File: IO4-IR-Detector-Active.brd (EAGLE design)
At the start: 50 x 50 mm, 32 parts, among them Q1 NPN-2222, Q2 NPN-2222, Q3 NPN-2222, Q4 NPN-2222

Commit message: panelized
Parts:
- C3: device SPCoast:E2-5 -> SPCoast:0810-CAP
- moved LED1 7.62 mm to (14.0, 3.81), turned to 270 degrees
- moved LED4 7.62 mm to (6.35, 3.81), turned to 270 degrees
- moved R12 7.62 mm to (6.35, 8.26)
- moved R9 7.62 mm to (14.0, 8.26)
- moved C3 4.84 mm to (38.6, 4.83)
- moved LED2 2.54 mm to (11.4, 3.81), turned to 270 degrees
- moved LED3 2.54 mm to (8.89, 3.81), turned to 270 degrees
- moved R10 2.54 mm to (11.4, 8.26)
- moved R11 2.54 mm to (8.89, 8.26)
- moved Q2 1.42 mm to (29.2, 39.4), turned to 180 degrees
- moved R2 1.27 mm to (40.0, 35.6)
- moved R6 1.27 mm to (34.9, 35.6)
- moved JP2 1.27 mm to (42.5, 31.8)
- moved JP3 1.27 mm to (42.5, 21.6)
- moved JP4 1.27 mm to (42.5, 11.4)
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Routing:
- net GND: track 31.4 -> 54.8 mm, vias 8 -> 4
- net V+: track 164.3 -> 175.8 mm
- net L1: track 17.6 -> 10.7 mm
- net L2: track 20.6 -> 14.3 mm
- net L3: track 21.5 -> 17.9 mm
- net IR4: track 58.8 -> 56.0 mm
- net IRSIG4: track 45.2 -> 43.0 mm
- net IRSIG1: track 34.5 -> 32.6 mm, vias 1 -> 2
- net IR3: track 51.9 -> 50.0 mm
- net IRSIG3: track 28.6 -> 27.5 mm
- net IRDRIVE1: track 11.1 -> 10.0 mm
- net IR2: track 41.6 -> 40.9 mm
- net IRDRIVE2: track 11.6 -> 10.9 mm
- net IRSIG2: track 18.7 -> 19.2 mm
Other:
- outline, holes or cut-outs redrawn
- board text added: "C1"
- board text added: "C2"
- board text added: "C3"
- board text added: "CON1"
- board text added: "JP1"
- board text added: "JP2"
- board text added: "JP3"
- board text added: "JP4"
- board text added: "LED1"
- board text added: "LED2"
- board text added: "LED3"
- board text added: "LED4"
- board text added: "LED5"
- board text added: "Q1"
- board text added: "Q2"
- board text added: "Q3"
- board text added: "Q4"
- board text added: "R1"
- board text added: "R10"
- board text added: "R11"
- board text added: "R12"
- board text added: "R14"
- board text added: "R2"
- board text added: "R3"
- board text added: "R4"
- board text added: "R5"
- board text added: "R6"
- board text added: "R7"
- board text added: "R8"
- board text added: "R9"

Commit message: added values for connectors
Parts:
- CON1: value (none) -> RJ12/6
- JP1, JP2, JP3, JP4: value (none) -> 0.100
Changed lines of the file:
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@@
 <attribute name="VALUE" x="33.782" y="44.831" size="0.8128" layer="27" rot="R180"/>
 </element>
-<element name="JP1" library="SPCoast" package="1X04_LOCK" value="" x="42.545" y="41.91" smashed="yes" rot="R180">
+<element name="JP1" library="SPCoast" package="1X04_LOCK" value="0.100" x="42.545" y="41.91" smashed="yes" rot="R180">
 <attribute name="NAME" x="43.8912" y="44.9072" size="0.8128" layer="25" ratio="10" rot="R180"/>
 <attribute name="VALUE" x="43.815" y="45.085" size="1.27" layer="27" rot="R180"/>
 </element>
-<element name="JP2" library="SPCoast" package="1X04_LOCK" value="" x="42.545" y="31.75" smashed="yes" rot="R180">
+<element name="JP2" library="SPCoast" package="1X04_LOCK" value="0.100" x="42.545" y="31.75" smashed="yes" rot="R180">
 <attribute name="NAME" x="44.3992" y="34.4932" size="0.8128" layer="25" ratio="10" rot="R180"/>
 <attribute name="VALUE" x="43.815" y="34.925" size="1.27" layer="27" rot="R180"/>
@@
 <attribute name="VALUE" x="33.782" y="24.384" size="0.8128" layer="27" rot="R180"/>
 </element>
-<element name="JP3" library="SPCoast" package="1X04_LOCK" value="" x="42.545" y="21.59" smashed="yes" rot="R180">
+<element name="JP3" library="SPCoast" package="1X04_LOCK" value="0.100" x="42.545" y="21.59" smashed="yes" rot="R180">
 <attribute name="NAME" x="44.3992" y="24.3332" size="0.8128" layer="25" ratio="10" rot="R180"/>
 <attribute name="VALUE" x="43.815" y="24.765" size="1.27" layer="27" rot="R180"/>
 </element>
-<element name="JP4" library="SPCoast" package="1X04_LOCK" value="" x="42.545" y="11.43" smashed="yes" rot="R180">
+<element name="JP4" library="SPCoast" package="1X04_LOCK" value="0.100" x="42.545" y="11.43" smashed="yes" rot="R180">
 <attribute name="NAME" x="44.1452" y="14.4272" size="0.8128" layer="25" ratio="10" rot="R180"/>
 <attribute name="VALUE" x="43.815" y="14.605" size="1.27" layer="27" rot="R180"/>
@@
 <attribute name="VALUE" x="16.51" y="44.831" size="1.016" layer="27" rot="R180"/>
 </element>
-<element name="CON1" library="SPCoast" package="RJ25-PANEL" value="" x="22.86" y="3.175">
+<element name="CON1" library="SPCoast" package="RJ25-PANEL" value="RJ12/6" x="22.86" y="3.175">
 <attribute name="AMP" value="520250-3" x="22.86" y="3.175" size="1.778" layer="27" font="vector" ratio="10" display="off"/>
 <attribute name="OPL" value="none" x="22.86" y="3.175" size="1.778" layer="27" font="vector" ratio="10" display="off"/>

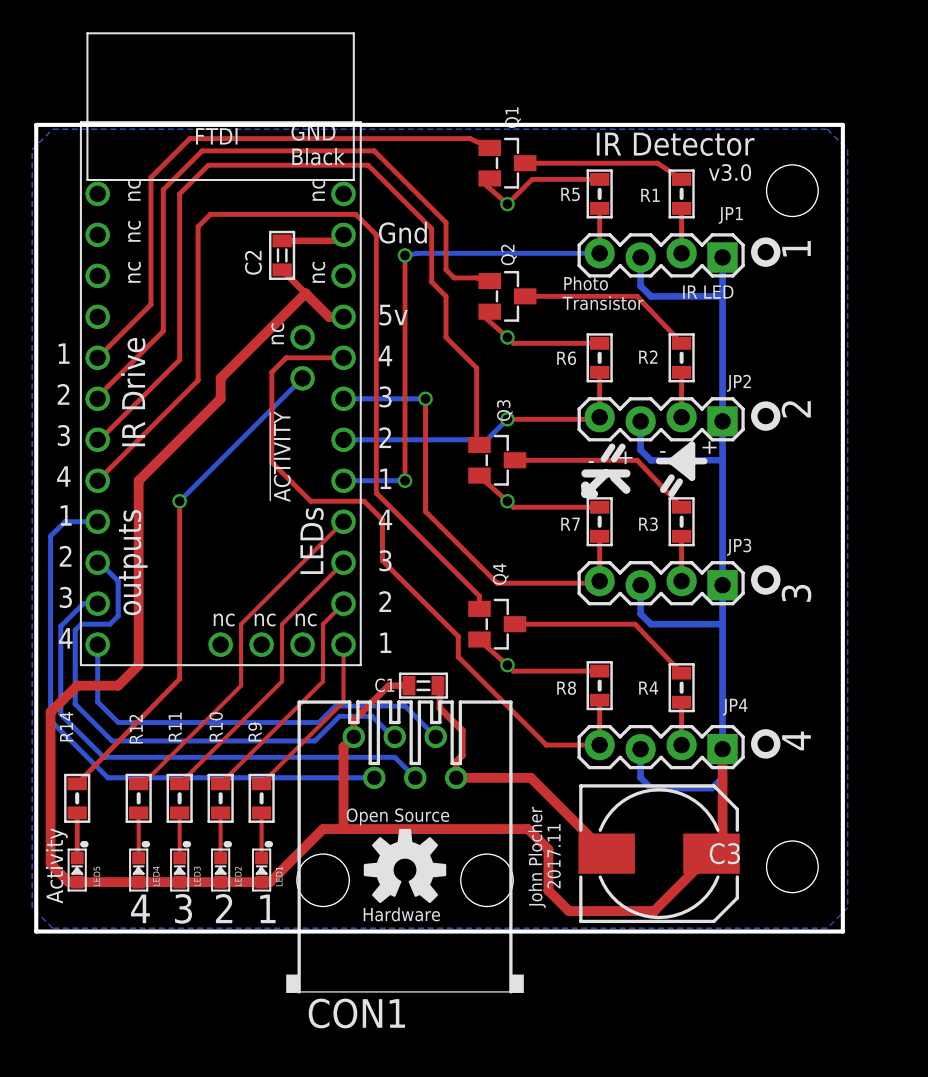
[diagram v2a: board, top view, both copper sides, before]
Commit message: normalized values
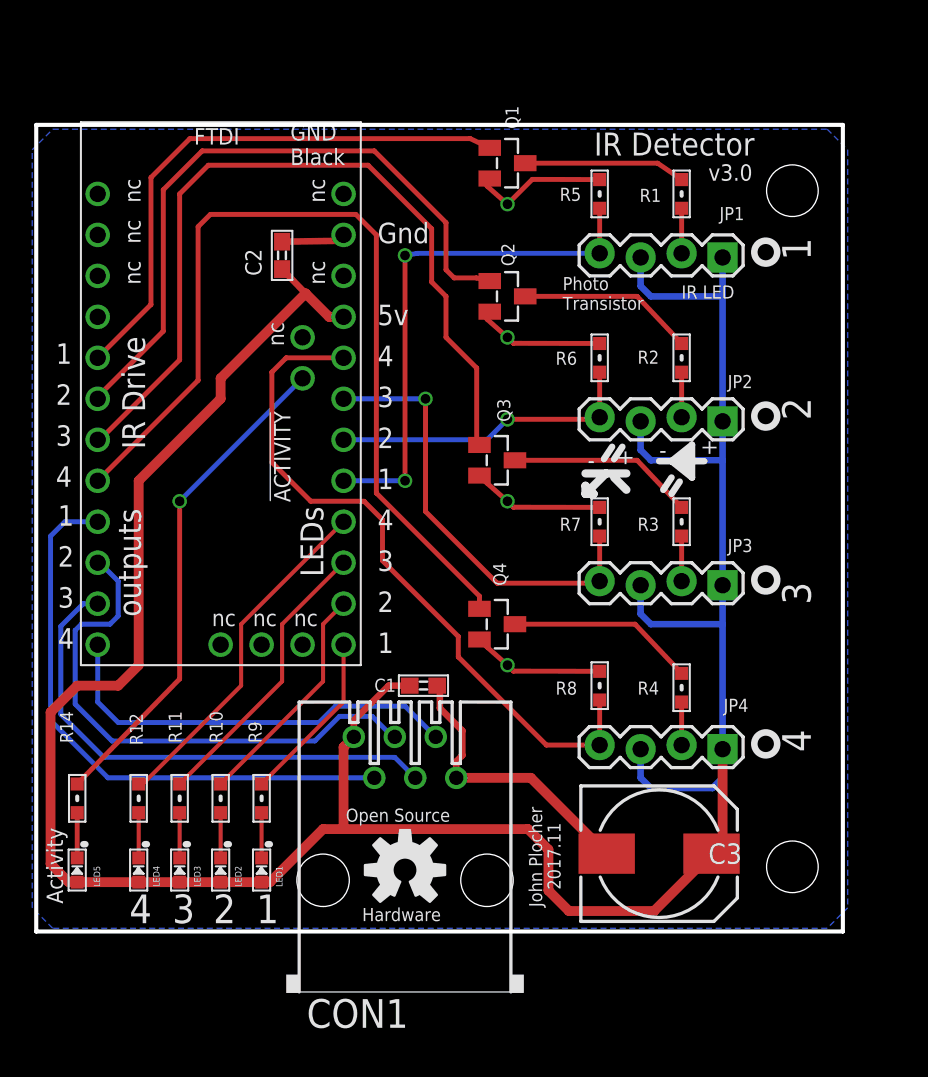
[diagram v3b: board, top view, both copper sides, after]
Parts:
- ARDUINO1: value ARDUINO-PRO-MINIDAVESROBOT -> DAVEK
- C1, C2: device SPCoast:0805-CAP -> SPCoast:0603-CAP
- R1, R10, R11, R12, R14, R2, R3, R4, R5, R6, R7, R8, R9: device SPCoast:0805-RES -> SPCoast:0603-RES

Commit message: make room for conveyer fingers
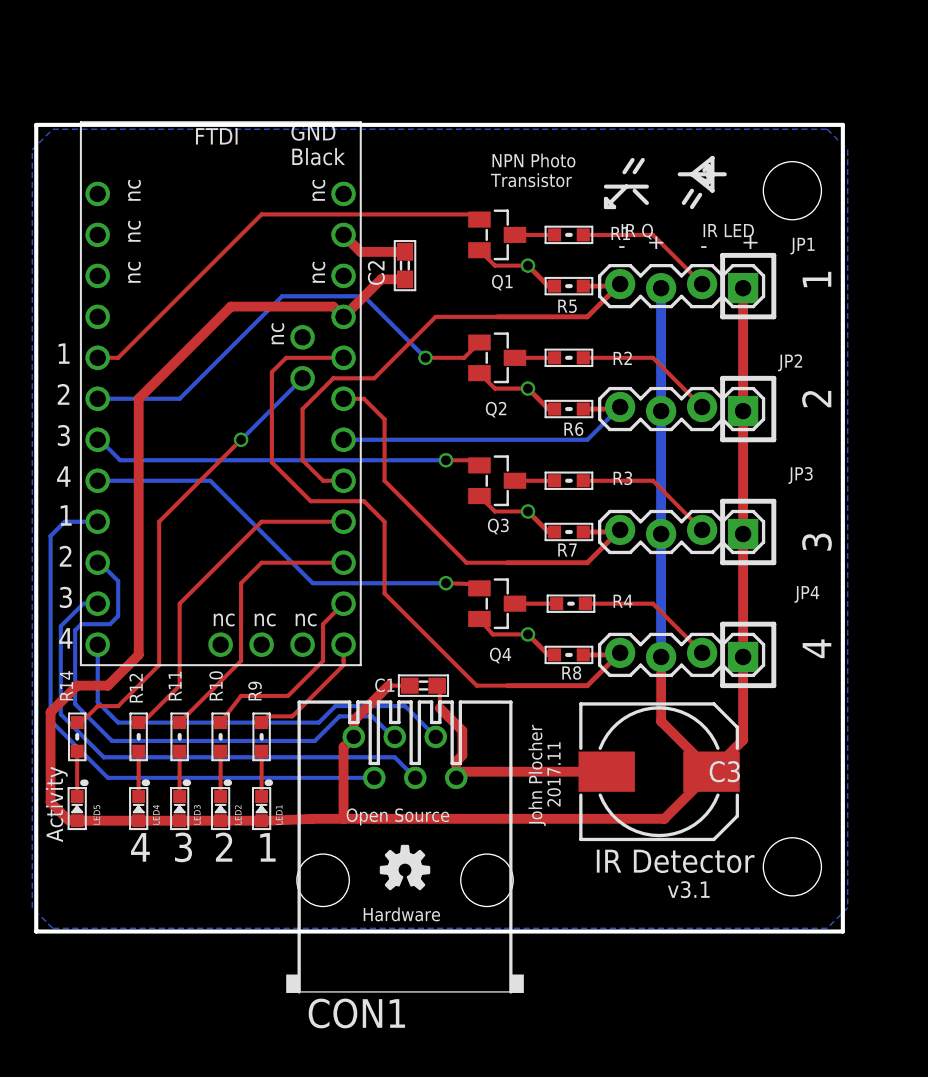
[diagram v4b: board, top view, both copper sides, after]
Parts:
- OSH_LOGO: value OSHW-LOGOM -> DOC-OSHW-LOGO-S; device SparkFun:OSHW-LOGO-M -> SPCoast:OSHW-LOGO-S
- R1, R2, R3, R4: value 1k0 -> 330R
- R14: value 2k0 -> 5k0
- moved R4 8.61 mm to (33.1, 20.3), turned to 0 degrees
- moved C2 7.65 mm to (22.9, 41.3)
- moved R1 7.43 mm to (33.0, 43.2), turned to 0 degrees
- moved R3 7.43 mm to (33.0, 27.9), turned to 0 degrees
- moved R2 6.98 mm to (33.0, 35.6), turned to 0 degrees
- moved R5 6.02 mm to (33.0, 40.0), turned to 180 degrees
- moved JP4 5.85 mm to (43.8, 17.1)
- moved C3 5.08 mm to (38.6, 9.91)
- moved Q1 4.49 mm to (28.6, 43.2)
- moved Q2 3.86 mm to (28.6, 35.6)
- moved LED1 3.81 mm to (14.0, 7.62)
- moved LED2 3.81 mm to (11.4, 7.62)
- moved LED3 3.81 mm to (8.89, 7.62)
- moved LED4 3.81 mm to (6.35, 7.62)
- moved LED5 3.81 mm to (2.54, 7.62)
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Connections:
- net V+ renamed VCC
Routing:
- net IR4: track 56.0 -> 26.3 mm, vias 0 -> 1
- net IR3: track 50.0 -> 24.4 mm, vias 0 -> 1
- net IR2: track 40.9 -> 28.3 mm, vias 0 -> 1
- net VCC: track 175.8 -> 163.9 mm
- net GND: track 54.8 -> 43.0 mm
- net IRDRIVE3: track 11.6 -> 2.46 mm
- net IRDRIVE4: track 11.6 -> 2.58 mm
- net IRDRIVE2: track 11.0 -> 2.46 mm
- net IRDRIVE1: track 10.0 -> 2.46 mm
- net IR1: track 34.7 -> 27.5 mm
- net N$4: track 2.79 -> 8.63 mm
- net N$3: track 2.79 -> 8.63 mm
- net N$5: track 2.67 -> 8.50 mm
- net N$2: track 2.79 -> 8.63 mm
- net L1: track 10.7 -> 7.82 mm
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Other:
- board text added: "#1"
- board text added: "#2"
- board text added: "#3"
- board text added: "#4"
- board text added: "+5v"
- board text added: "Auto compensates for changes in ambient light"
- board text added: "GND"
- board text added: "IR Detector - Active"
- board text added: "IR Q"
- board text added: "Infrared Emitter IR 940nm"
- board text added: "Infrared Emitters IR 940nm"
- board text added: "NPN Photo Transistor"
- board text added: "v3.1"
- board text removed: "!ACTIVITY"
- board text removed: "5v"
- board text removed: "Auto compensates for ambient light"
- board text removed: "Gnd"
- board text removed: "IR Drive"
- board text removed: "Infrared Emitters IR 940nm 34 deg Water Clear"
- board text removed: "LEDs"
- board text removed: "Photo Transistor"
- board text removed: "Solder Side"
- board text removed: "outputs"
- board text removed: "v3.0"
